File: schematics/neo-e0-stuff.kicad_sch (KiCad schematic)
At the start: 4 parts

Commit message: WIP
starting Page 2 : LSPC2
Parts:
- 7F: symbol 0-Custom-SNK:NEO-E0 -> 0-Custom-SNK:NEO-E0 (MV2F)
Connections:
- net A22Z: now reaches 7F.55 (A22I)
- net A23Z: now reaches 7F.56 (A23I)
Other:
- company: (none) -> SNK
- title: (none) -> NEO-EO shift registers
- moved on the sheet: 5EA, 5F, 5JC, 7F

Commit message: update readme
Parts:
- renumbered 5E to 5E1, 5F to 5F1, 5J to 5J1, 7F to 7F1
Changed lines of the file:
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@@
   (symbol (lib_id "74xx:74LS259") (at 64.77 53.34 0) (unit 1)
     (in_bom yes) (on_board yes) (dnp no)
-    (property "Reference" "5F" (at 57.15 39.37 0)
+    (property "Reference" "5F1" (at 57.15 39.37 0)
       (effects (font (size 1.27 1.27)) (justify left))
     )
@@
       (project "MVS"
         (path "/8d0803ab-15ed-47a7-8dcb-ab27dc5b29c2/a36cda8b-8f55-42e5-b1dc-011a6eeffdb5"
-          (reference "5F") (unit 1)
+          (reference "5F1") (unit 1)
         )
       )
@@
   (symbol (lib_id "74xx:74HC04") (at 111.76 55.88 0) (unit 1)
     (in_bom yes) (on_board yes) (dnp no)
-    (property "Reference" "5E" (at 107.95 50.8 0)
+    (property "Reference" "5E1" (at 107.95 50.8 0)
       (effects (font (size 1.27 1.27)))
     )
@@
       (project "MVS"
         (path "/8d0803ab-15ed-47a7-8dcb-ab27dc5b29c2/a36cda8b-8f55-42e5-b1dc-011a6eeffdb5"
-          (reference "5E") (unit 1)
+          (reference "5E1") (unit 1)
         )
       )
@@
   (symbol (lib_id "74xx:74HC04") (at 113.03 83.82 0) (unit 3)
     (in_bom yes) (on_board yes) (dnp no)
-    (property "Reference" "5J" (at 109.22 78.74 0)
+    (property "Reference" "5J1" (at 109.22 78.74 0)
       (effects (font (size 1.27 1.27)))
     )
@@
       (project "MVS"
         (path "/8d0803ab-15ed-47a7-8dcb-ab27dc5b29c2/a36cda8b-8f55-42e5-b1dc-011a6eeffdb5"
-          (reference "5J") (unit 3)
+          (reference "5J1") (unit 3)
         )
       )
@@
   (symbol (lib_id "0-Custom-SNK:NEO-E0 (MV2F)") (at 186.69 63.5 0) (unit 1)
     (in_bom yes) (on_board yes) (dnp no)
-    (property "Reference" "7F" (at 175.26 16.51 0)
+    (property "Reference" "7F1" (at 175.26 16.51 0)
       (effects (font (size 1.27 1.27)))
     )
@@
       (project "MVS"
         (path "/8d0803ab-15ed-47a7-8dcb-ab27dc5b29c2/a36cda8b-8f55-42e5-b1dc-011a6eeffdb5"
-          (reference "7F") (unit 1)
-        )
-      )
+          (reference "7F1") (unit 1)
+        )
+      )

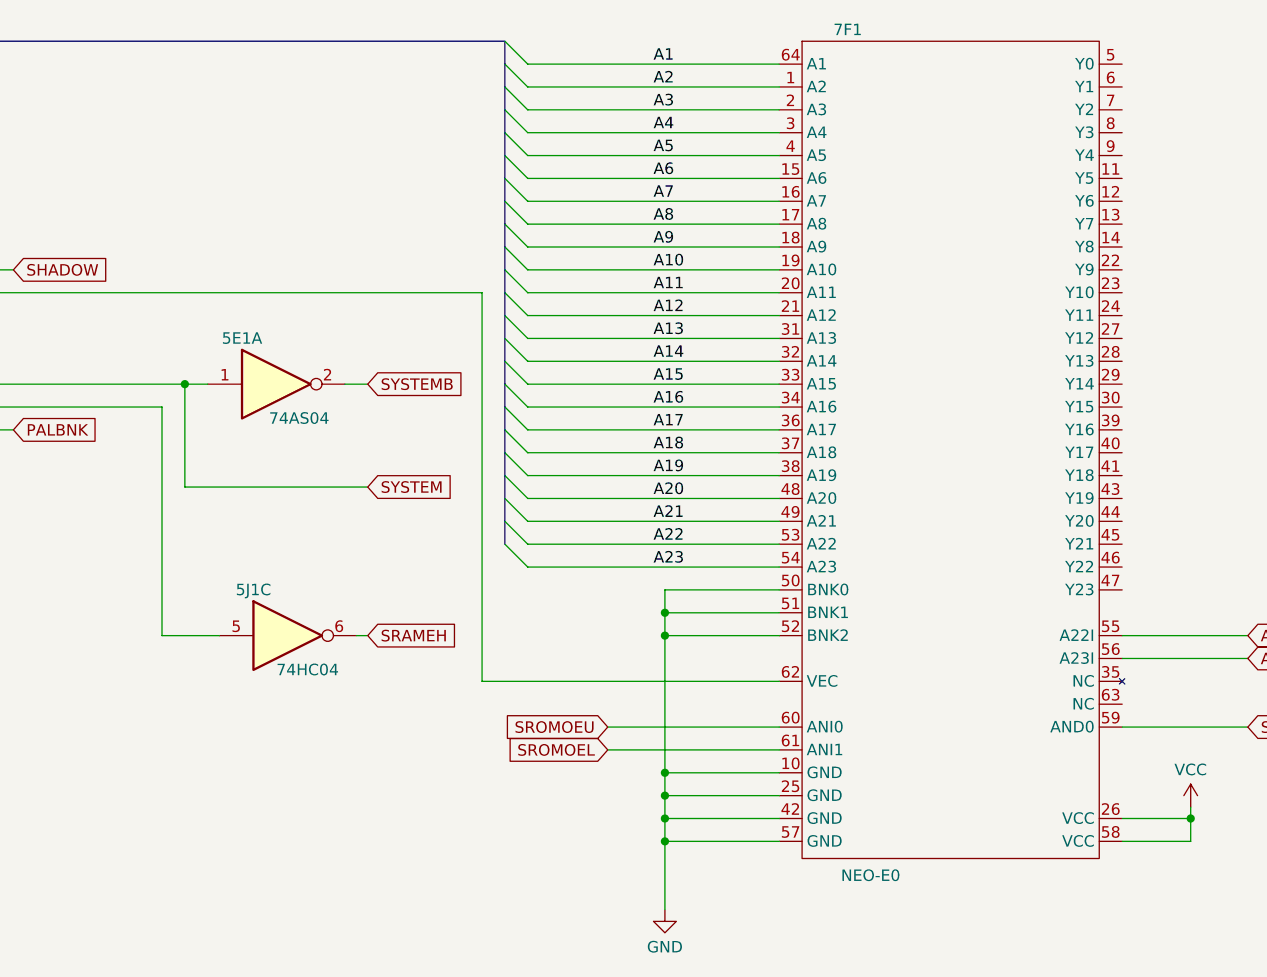
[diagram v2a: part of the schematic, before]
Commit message: update "main" schematics
Adding LSPC2-A2, NEO-B1, L0 ROM
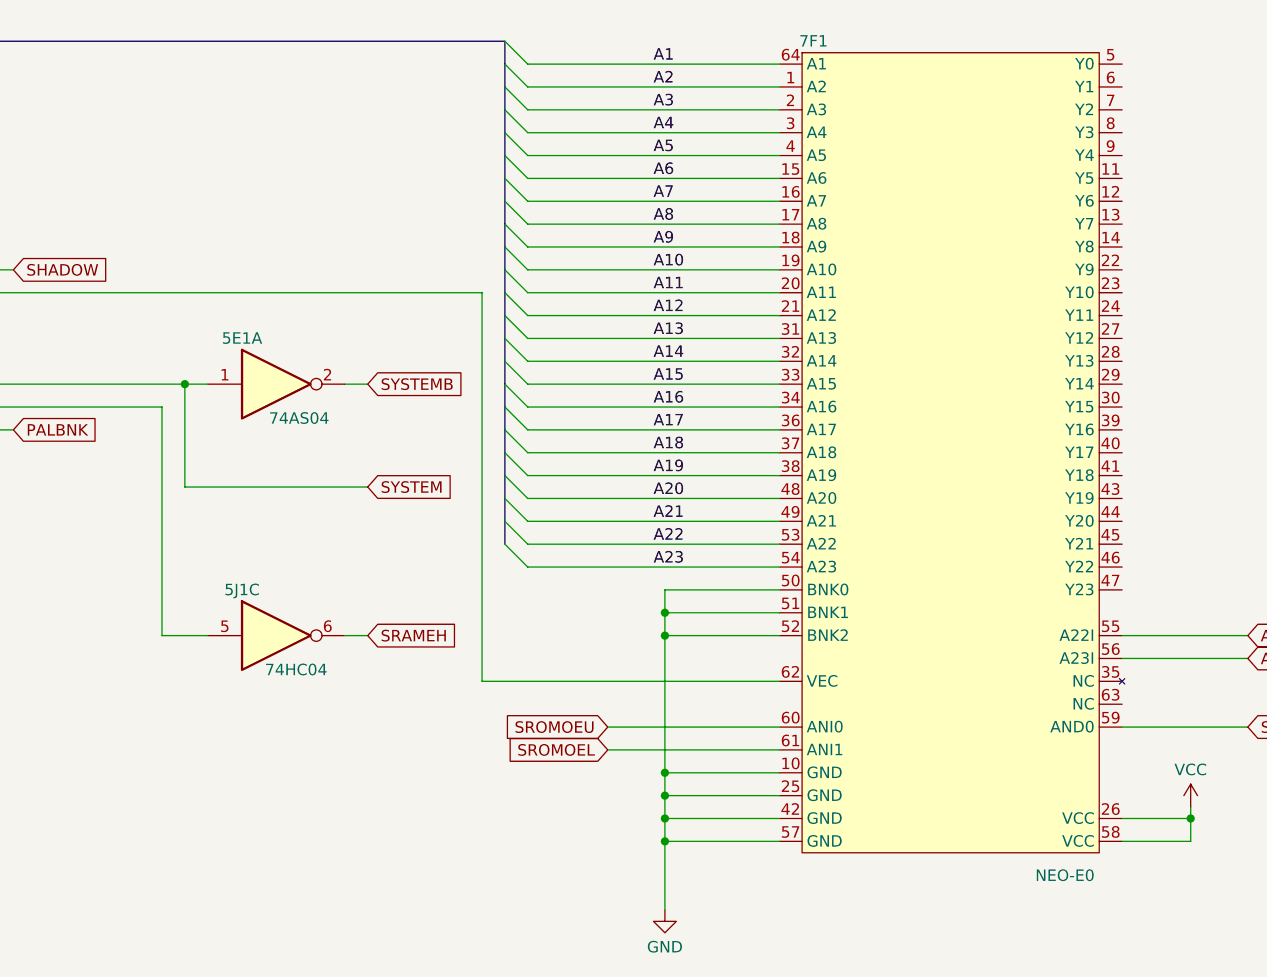
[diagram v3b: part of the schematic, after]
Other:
- moved on the sheet: 5J1C
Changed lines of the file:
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@@
     (stroke (width 0) (type default))
   )
-  (wire (pts (xy 99.06 83.82) (xy 105.41 83.82))
+  (wire (pts (xy 99.06 83.82) (xy 104.14 83.82))
     (stroke (width 0) (type default))
   )
@@
     (stroke (width 0) (type default))
   )
-  (wire (pts (xy 120.65 83.82) (xy 121.92 83.82))
+  (wire (pts (xy 119.38 83.82) (xy 121.92 83.82))
     (stroke (width 0) (type default))
   )
@@
     )
   )
-  (symbol (lib_id "74xx:74HC04") (at 113.03 83.82 0) (unit 3)
+  (symbol (lib_id "74xx:74HC04") (at 111.76 83.82 0) (unit 3)
     (in_bom yes) (on_board yes) (dnp no)
-    (property "Reference" "5J1" (at 109.22 78.74 0)
-      (effects (font (size 1.27 1.27)))
-    )
-    (property "Value" "74HC04" (at 111.76 87.63 0)
-      (effects (font (size 1.27 1.27)) (justify left))
-    )
-    (property "Footprint" "" (at 113.03 83.82 0)
-      (effects (font (size 1.27 1.27)) hide)
-    )
-    (property "Datasheet" "https://assets.nexperia.com/documents/data-sheet/74HC_HCT04.pdf" (at 113.03 83.82 0)
+    (property "Reference" "5J1" (at 107.95 78.74 0)
+      (effects (font (size 1.27 1.27)))
+    )
+    (property "Value" "74HC04" (at 110.49 87.63 0)
+      (effects (font (size 1.27 1.27)) (justify left))
+    )
+    (property "Footprint" "" (at 111.76 83.82 0)
+      (effects (font (size 1.27 1.27)) hide)
+    )
+    (property "Datasheet" "https://assets.nexperia.com/documents/data-sheet/74HC_HCT04.pdf" (at 111.76 83.82 0)
       (effects (font (size 1.27 1.27)) hide)
     )
@@
   (symbol (lib_id "0-Custom-SNK:NEO-E0 (MV2F)") (at 186.69 63.5 0) (unit 1)
     (in_bom yes) (on_board yes) (dnp no)
-    (property "Reference" "7F1" (at 175.26 16.51 0)
-      (effects (font (size 1.27 1.27)))
-    )
-    (property "Value" "NEO-E0" (at 177.8 110.49 0)
-      (effects (font (size 1.27 1.27)))
-    )
+    (property "Reference" "7F1" (at 171.45 17.78 0)
+      (effects (font (size 1.27 1.27)))
+    )
+    (property "Value" "NEO-E0" (at 199.39 110.49 0)
+      (effects (font (size 1.27 1.27)))
+    )

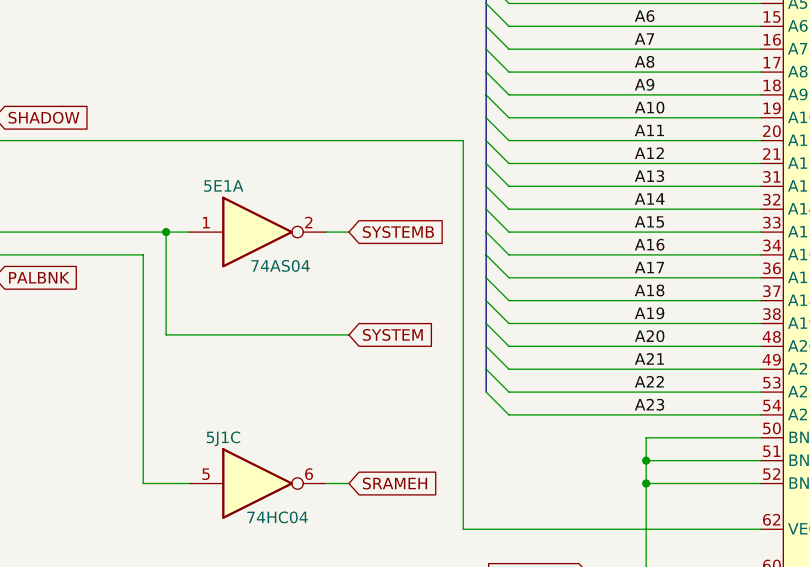
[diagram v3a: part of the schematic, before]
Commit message: Complete Page 2 (LSPC2-A2)
Complete "Main" page LSPC2, NEO-IO, NEO-B1, NEO-ZMC2 & SFix Rom LO Rom
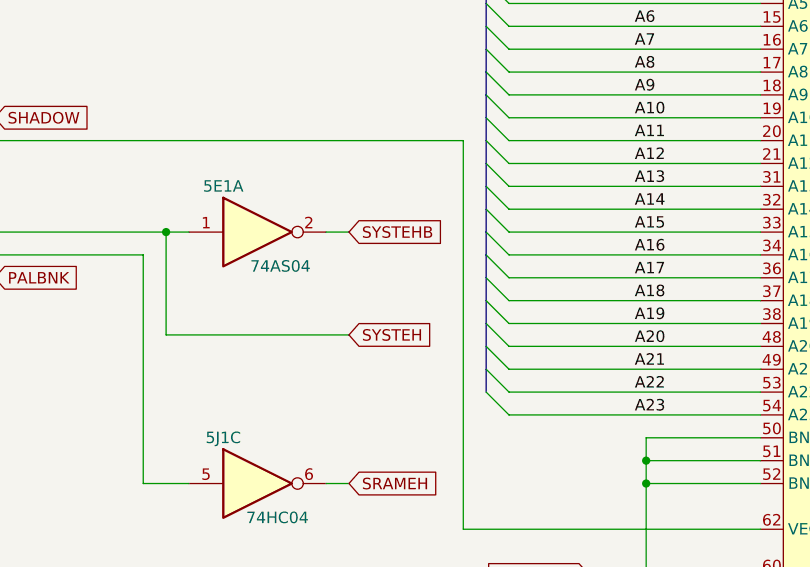
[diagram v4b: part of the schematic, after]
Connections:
- net SYSTEM renamed SYSTEH
- net SYSTEMB renamed SYSTEHB
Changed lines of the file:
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@@
     )
   )
-  (global_label "SYSTEMB" (shape input) (at 121.92 55.88 0) (fields_autoplaced)
+  (global_label "SYSTEHB" (shape input) (at 121.92 55.88 0) (fields_autoplaced)
     (effects (font (size 1.27 1.27)) (justify left))
     (property "Intersheetrefs" "${INTERSHEET_REFS}" (at 133.2508 55.88 0)
@@
     )
   )
-  (global_label "SYSTEM" (shape input) (at 121.92 67.31 0) (fields_autoplaced)
+  (global_label "SYSTEH" (shape input) (at 121.92 67.31 0) (fields_autoplaced)
     (effects (font (size 1.27 1.27)) (justify left))
     (property "Intersheetrefs" "${INTERSHEET_REFS}" (at 131.9808 67.31 0)

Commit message: Complete pages 1-4
completion of pages 1 to 4
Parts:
- added 5J: 74HC04, symbol 74xx:74HC04
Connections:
- net VCC: now also 5J.1, 5J.11, 5J.13, 5J.3, 5J.9

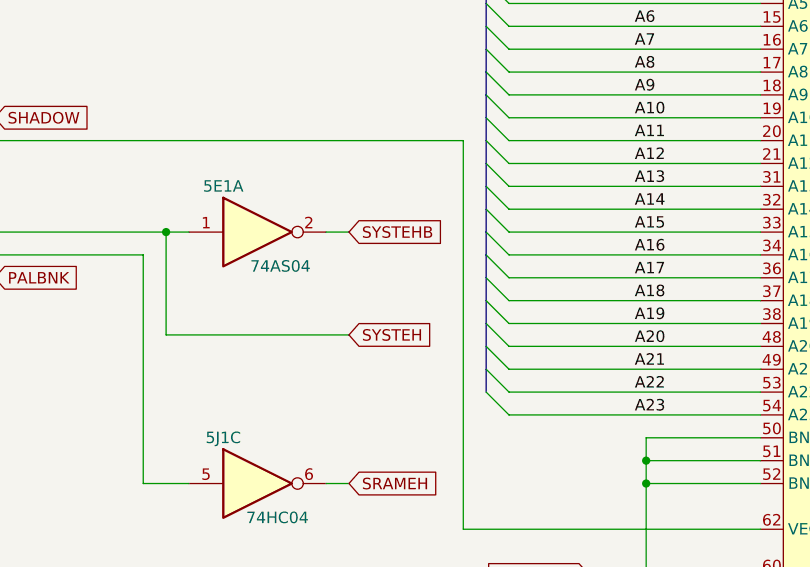
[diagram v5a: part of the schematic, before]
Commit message: Audio Amp + player's button LED & marquee + Coins Up + 45% raiser card connectors
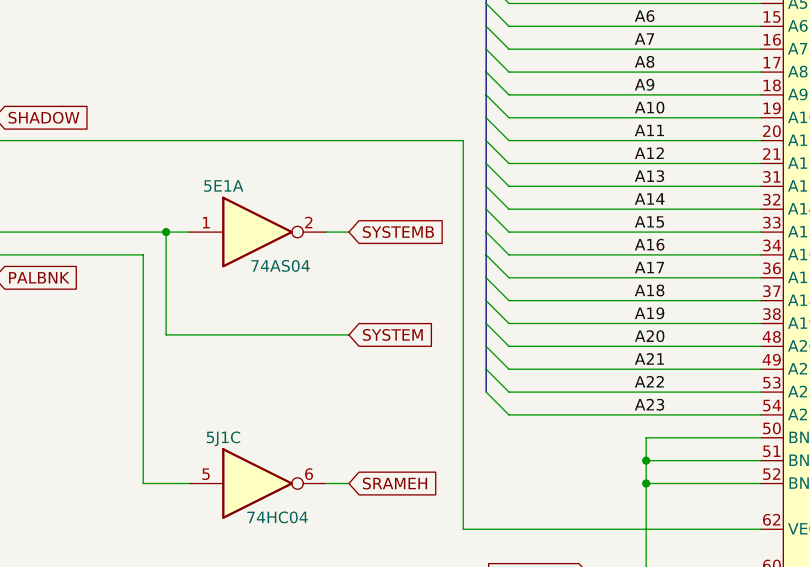
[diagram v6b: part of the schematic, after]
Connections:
- net SYSTEH renamed SYSTEM
- net SYSTEHB renamed SYSTEMB
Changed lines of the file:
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@@
     )
   )
-  (global_label "SYSTEHB" (shape input) (at 121.92 55.88 0) (fields_autoplaced)
+  (global_label "SYSTEMB" (shape input) (at 121.92 55.88 0) (fields_autoplaced)
     (effects (font (size 1.27 1.27)) (justify left))
     (property "Intersheetrefs" "${INTERSHEET_REFS}" (at 133.2508 55.88 0)
@@
     )
   )
-  (global_label "SYSTEH" (shape input) (at 121.92 67.31 0) (fields_autoplaced)
+  (global_label "SYSTEM" (shape input) (at 121.92 67.31 0) (fields_autoplaced)
     (effects (font (size 1.27 1.27)) (justify left))
     (property "Intersheetrefs" "${INTERSHEET_REFS}" (at 131.9808 67.31 0)
